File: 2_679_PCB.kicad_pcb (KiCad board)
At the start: 2 copper layers, 101.6 x 76.2 mm, 113 parts, among them J1 POWER_IN, J10 DC Motor Header, J11 DC Motor Header, J12 DC Motor Header, J13 DC Motor Header, J14 Conn_01x06_Female, J15 Conn_01x06_Female, J16 Conn_01x06_Female, J17 Conn_01x06_Female, J18 I2C_3V3, J19 Servo Header, J2 ARDUINO_HEADER_1, J20 Servo Header, J21 Servo Header, J22 Servo Header, J23 Servo Header, J24 Servo Header, J25 Servo Header, J26 Servo Header, J27 RC IN, J28 NEOPIXEL, J29 MPU6050, J3 ARDUINO_HEADER_2, J30 USB_C_Receptacle_USB2.0, J4 I2C_5V, J5 POWER_OUT, J6 DC Motor Header, J7 DC Motor Header, J8 DC Motor Header, J9 DC Motor Header, SW1 SW_SPST, SW2 SW_Push_Open, SW3 SW_P3, SW4 SW_P4, SW5 SW_SPST, U1 SP7652ER-L/TR, U2 AON6558, U3 LMV331, U4 TCA9517DR, U5 AMS1117-5.0, U6 IP2721, U7 BU4SU69G2

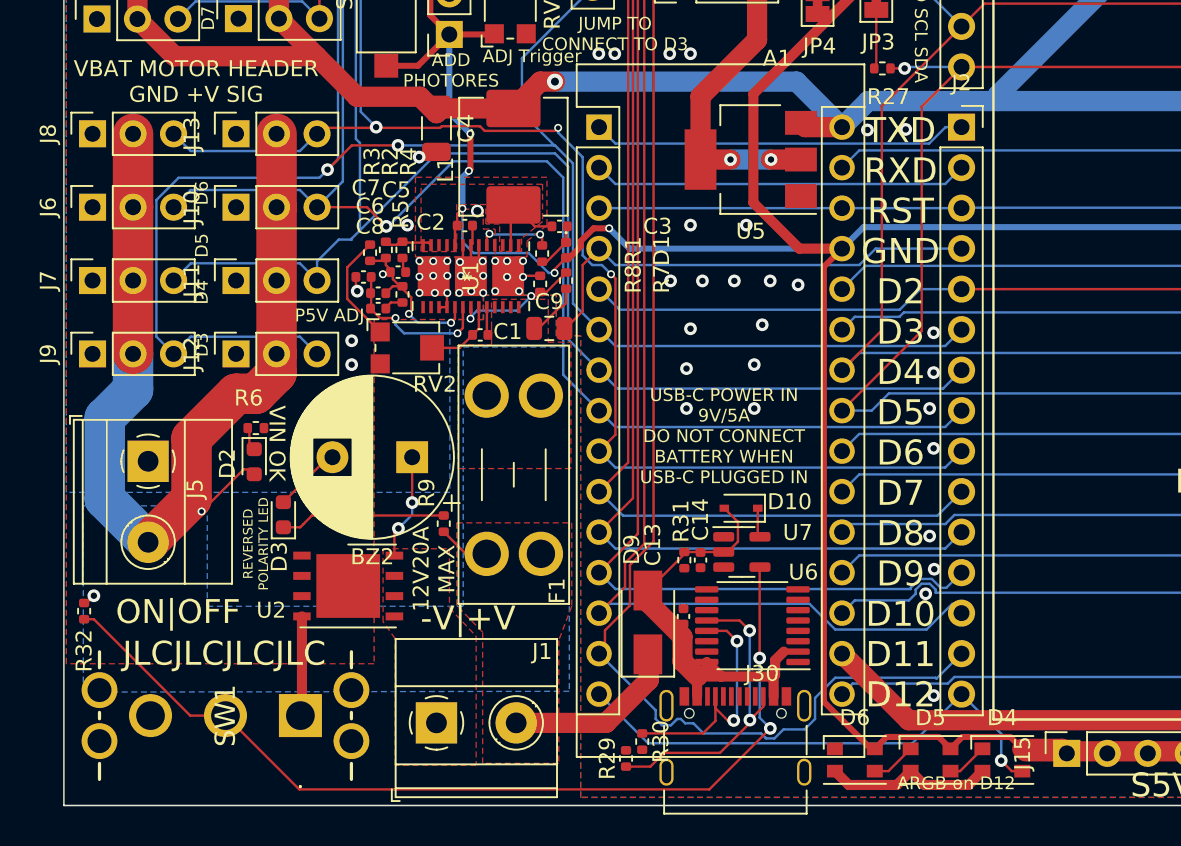
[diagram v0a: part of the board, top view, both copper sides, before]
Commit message: fully defined states for inverter
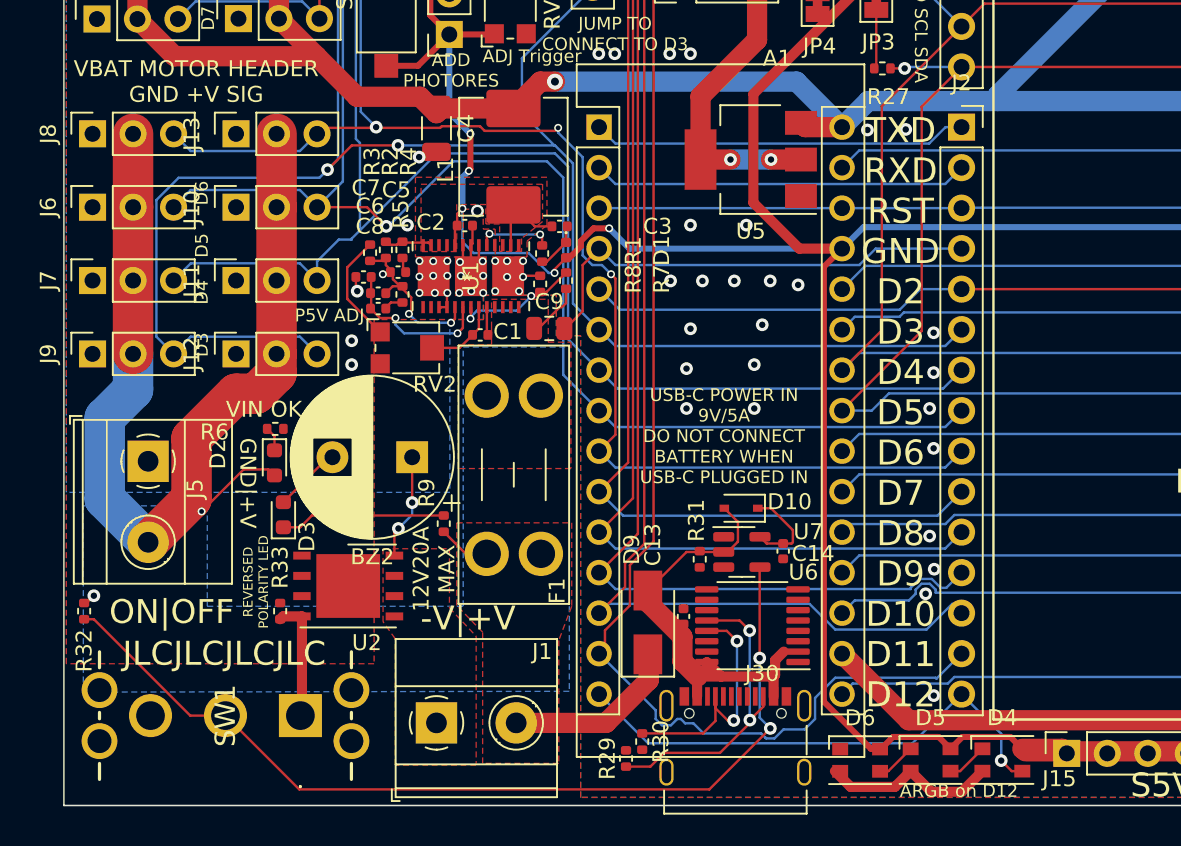
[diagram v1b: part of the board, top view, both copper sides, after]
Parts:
- added G***: LOGO, Logos:pika, B.Cu at (180.5, 117.6)
- added R33: 68K, Resistor_SMD:R_0402_1005Metric, F.Cu at (115.3, 140.2)
- moved C14 5.21 mm to (146.8, 136.4)
- moved D2 1.27 mm to (114.9, 130.9)
- moved R6 1.22 mm to (115.0, 128.8)
- moved R31 0.97 mm to (141.6, 137.0)
- moved D6 0.33 mm to (151.6, 149.6)
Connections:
- C14 pad 2: /VBUS_USBC -> Net-(D10-Pad1)
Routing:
- net Net-(D10-Pad1): track 1.85 -> 6.00 mm
- net VBUS: track 69.8 -> 71.5 mm
- net Net-(SW1-Pad1): track 6.26 -> 7.70 mm
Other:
- board text added: "GND|+V"
- board text added: "MIT / 2.679 / 2.007 Arduino Nano Carrier Board v1.1 2/16/22 WS github.com/wszeto9/2_679_PCB Input Voltage: 7-12V Max Output: 6A @ Vin"
- board text added: "Special note to Danny: This uses a SP7652ER-L/TR Buck IC You can stare at my board all you want but it's a buck IC which is allowed."
- board text added: "Steve: Your only constraint is 3in x 4 in Winnie: So you will print *anything* that fits in that footprint? Steve: Yes...<Looks at this board>"
- board text removed: "I WILL STOP PUTTING PASSIVES TOO CLOSE TO EACH OTHER I WILL STOP PUTTING PASSIVES TOO CLOSE TO EACH OTHER I WILL STOP PUTTING PASSIVES TOO CLOSE TO EACH OTHER I WILL STOP PUTTING PASSIVES TOO CLOSE TO EACH OTHER I WILL STOP PUTTING PASSIVES TOO CLOSE TO EACH OTHER I WILL STOP PUTTING PASSIVES TOO CLOSE TO EACH OTHER I WILL STOP PUTTING PASSIVES TOO CLOSE TO EACH OTHER I WILL STOP PUTTING PASSIVES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"
- board text removed: "MIT / 2.679 / 2.007 Arduino Nano Carrier Board v1.0 2/12/22 WS Input Voltage: 7-12V Max Output: 6A @ Vin"

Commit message: changed e-pads
changed e-pads
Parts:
- R1: value 5.1k -> 5.1R; footprint Resistor_SMD:R_0402_1005Metric -> Resistor_SMD:R_0603_1608Metric
- moved D6 2.24 mm to (153.9, 149.6), turned to -90 degrees
- moved D5 1.37 mm to (157.4, 149.6), turned to -90 degrees
- moved R8 0.82 mm to (131.8, 120.5)
- moved D4 0.43 mm to (161.0, 149.6), turned to -90 degrees
- moved R1 0.25 mm to (131.8, 118.0)
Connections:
- D4 pad 1: Net-(D4-Pad1) -> +5VD
- D4 pad 2: GND -> Net-(D4-Pad2)
- D4 pad 3: /D12 -> GND
- D4 pad 4: +5VD -> /D12
- D5 pad 1: Net-(D5-Pad1) -> +5VD
- D5 pad 2: GND -> Net-(D6-Pad4)
- D5 pad 3: Net-(D4-Pad1) -> GND
- D5 pad 4: +5VD -> Net-(D4-Pad2)
- D6 pad 1: unconnected-(D6-Pad1) -> +5VD
- D6 pad 2: GND -> unconnected-(D6-Pad2)
- D6 pad 3: Net-(D5-Pad1) -> GND
- D6 pad 4: +5VD -> Net-(D6-Pad4)
- U1 pad 28: GND -> /LX
- U1 pad 29: GND -> VBUS
- U2 pad 9: GND -> unconnected-(U2-Pad9)
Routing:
- net Net-(D4-Pad2): track 0.00 -> 3.39 mm
- net Net-(D6-Pad4): track 0.00 -> 3.39 mm
- net GND: track 110.1 -> 107.3 mm, vias 58 -> 45
- net Net-(D5-Pad1): track 2.83 -> 0.00 mm
- net Net-(D4-Pad1): track 2.58 -> 0.00 mm
- net +5VD: track 286.8 -> 289.2 mm
- net /BUCK_ENA: track 7.99 -> 8.75 mm

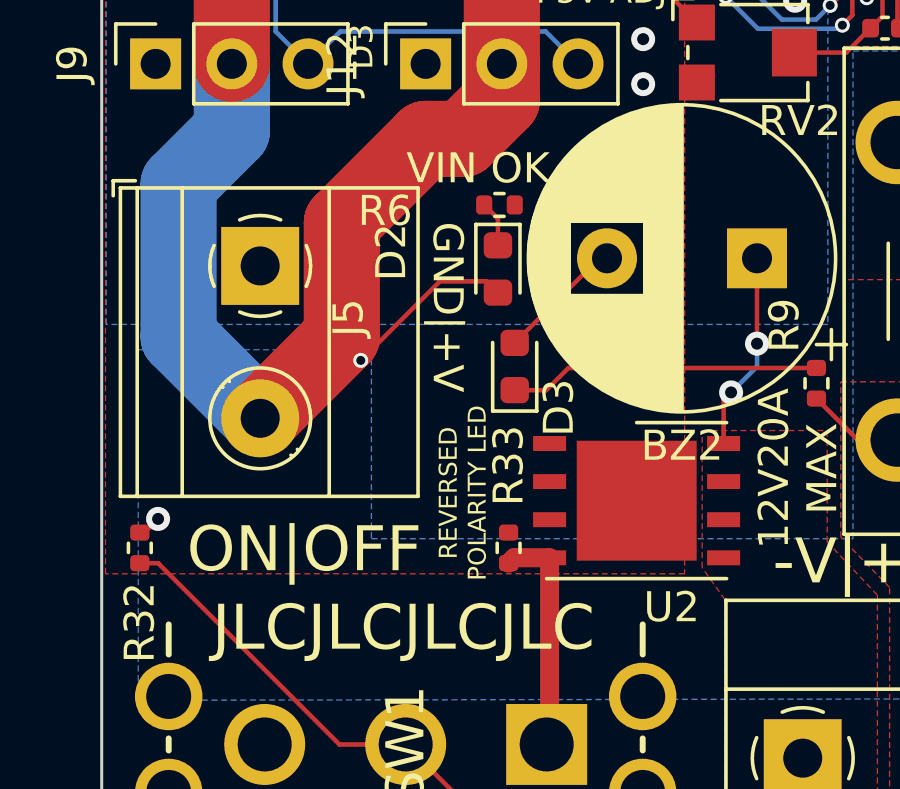
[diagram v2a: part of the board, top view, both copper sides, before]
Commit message: Doubled reverse bias LEDs
Prevents LEDs from blowing up from 5V max reverse bias
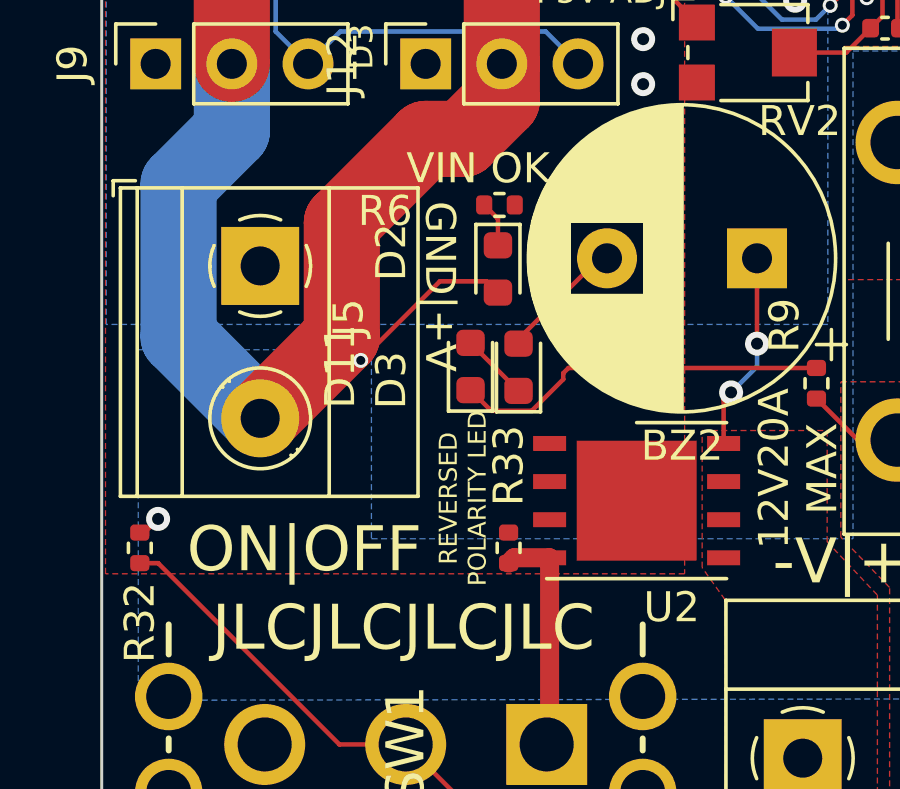
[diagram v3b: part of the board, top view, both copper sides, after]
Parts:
- added D11: LED, LED_SMD:LED_0603_1608Metric, F.Cu at (114.0, 134.2)
- moved D3 0.13 mm to (115.6, 134.2)
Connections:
- R9 pad 1: Net-(D3-Pad1) -> Net-(R9-Pad1)
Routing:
- net Net-(R9-Pad1): track 0.00 -> 12.5 mm
- net Net-(D3-Pad1): track 10.4 -> 2.26 mm
- net Net-(C3-Pad1): track 3.36 -> 0.00 mm
- net +5VD: track 289.2 -> 292.6 mm

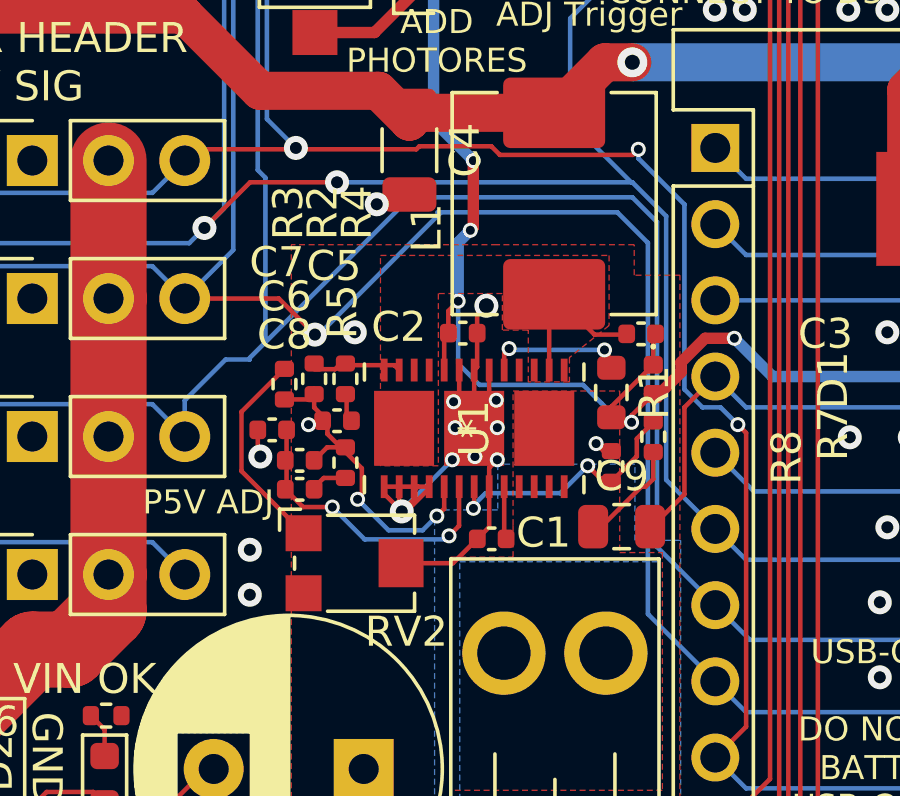
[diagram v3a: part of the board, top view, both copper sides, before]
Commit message: fixed DRC
trace was routed incorrectly
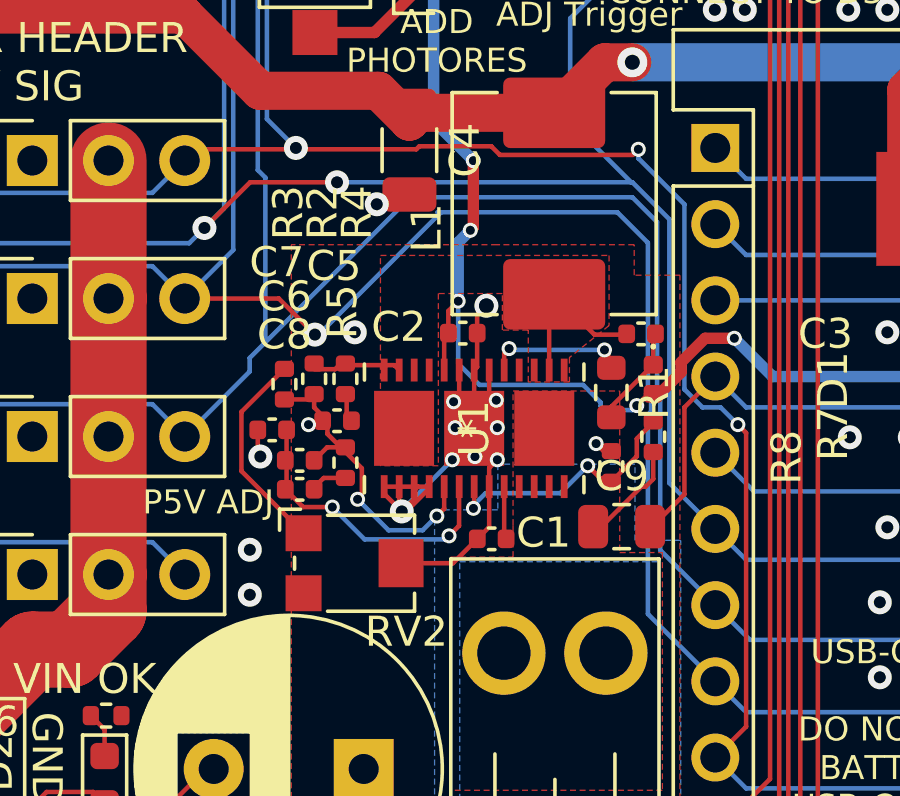
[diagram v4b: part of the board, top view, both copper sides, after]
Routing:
- net +5VD: track 292.6 -> 288.8 mm
- net Net-(C3-Pad1): track 0.00 -> 3.49 mm

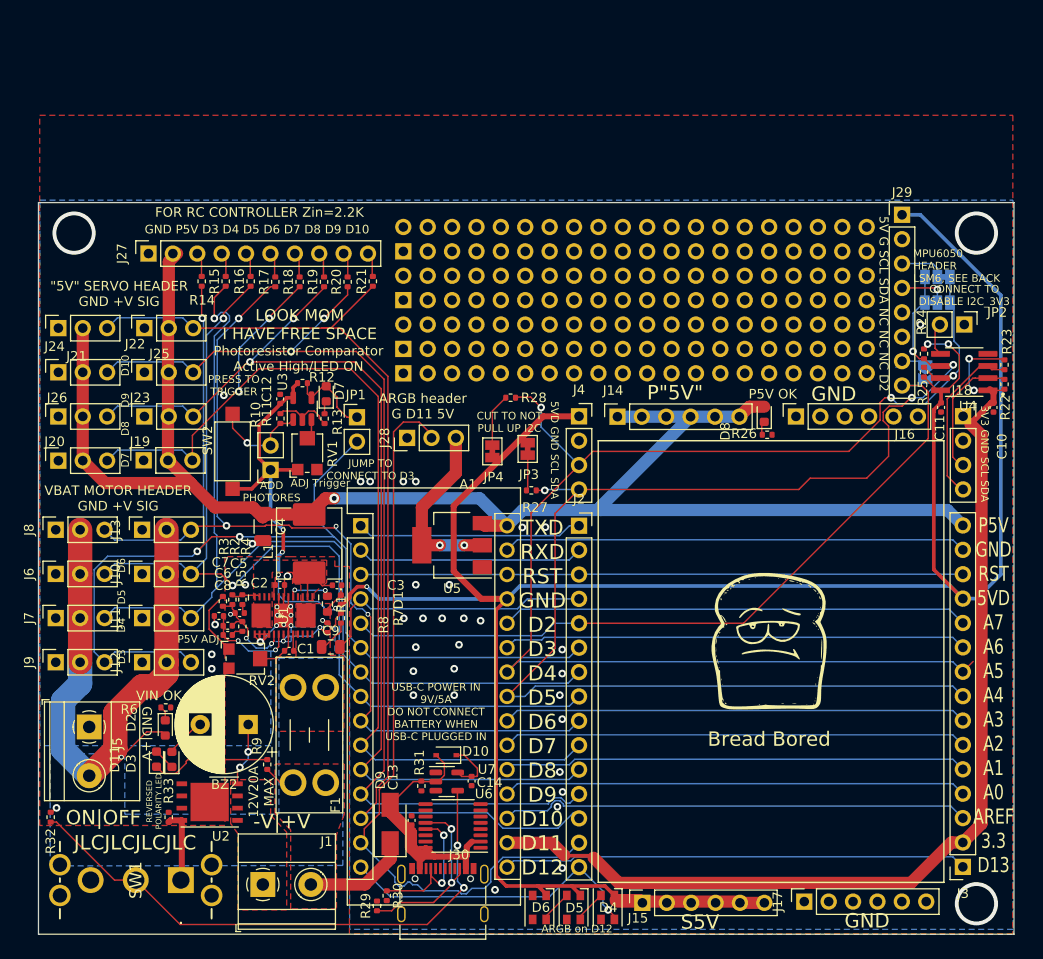
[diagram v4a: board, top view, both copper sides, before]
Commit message: added breakout boards
Added boards to increase space use of the board to 4x4"
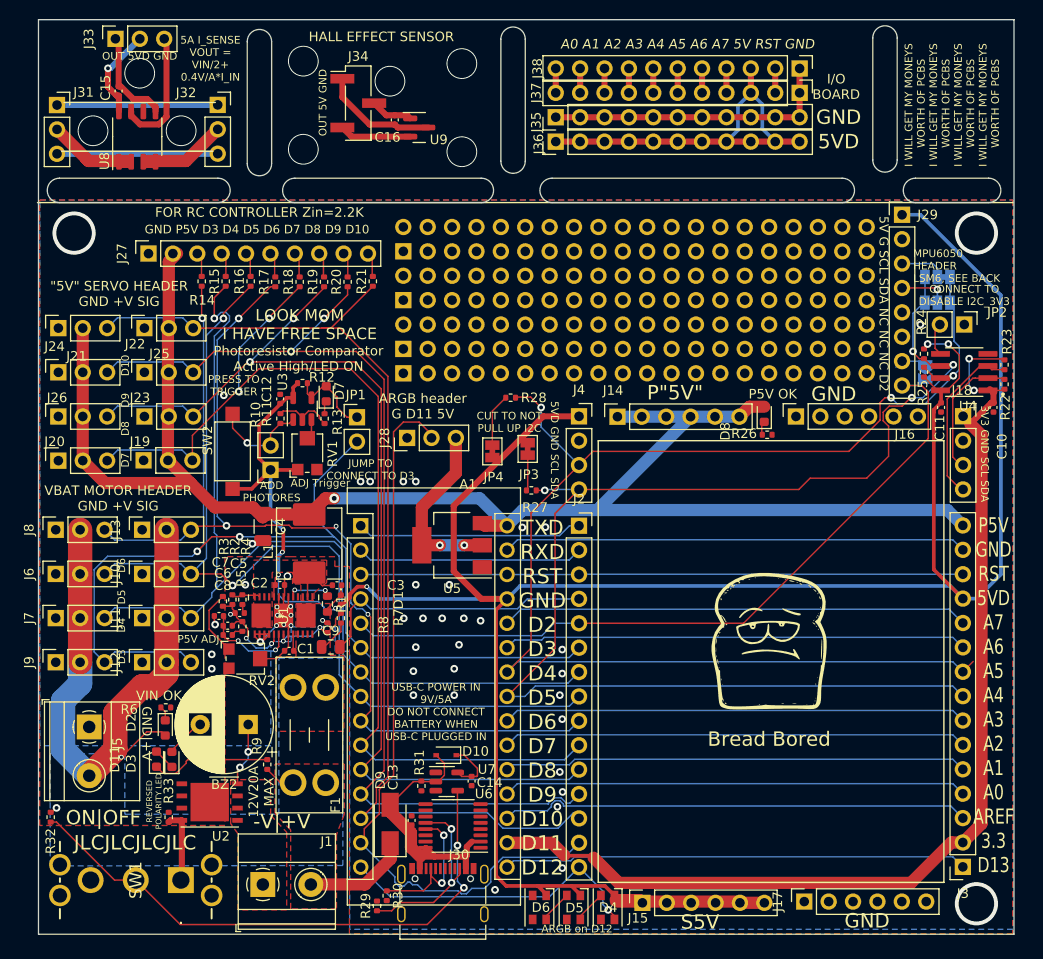
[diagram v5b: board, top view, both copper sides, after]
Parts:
- added C15: 0.1uF, Capacitor_SMD:C_0402_1005Metric, F.Cu at (110.1, 64.6)
- added C16: 0.1uF, Capacitor_SMD:C_0402_1005Metric, F.Cu at (138.8, 67.6)
- added J31: I_IN, Connector_PinSocket_2.54mm:PinSocket_1x03_P2.54mm_Vertical, F.Cu at (103.6, 66.0)
- added J32: I_OUT, Connector_PinSocket_2.54mm:PinSocket_1x03_P2.54mm_Vertical, F.Cu at (120.4, 66.0)
- added J33: D_OUT, Connector_PinSocket_2.54mm:PinSocket_1x03_P2.54mm_Vertical, F.Cu at (109.7, 59.1)
- added J34: HALL_OUT, Connector_PinHeader_2.54mm:PinHeader_1x03_P2.54mm_Vertical_SMD_Pin1Left, F.Cu at (135.0, 65.8)
- added J35: Conn_01x11_Male, Connector_PinHeader_2.54mm:PinHeader_1x11_P2.54mm_Vertical, F.Cu at (155.6, 67.3)
- added J36: Conn_01x11_Male, Connector_PinHeader_2.54mm:PinHeader_1x11_P2.54mm_Vertical, F.Cu at (155.6, 69.8)
- added J37: Conn_01x11_Male, Connector_PinHeader_2.54mm:PinHeader_1x11_P2.54mm_Vertical, F.Cu at (181.0, 64.8)
- added J38: Conn_01x11_Male, Connector_PinHeader_2.54mm:PinHeader_1x11_P2.54mm_Vertical, F.Cu at (181.0, 62.2)
- added U8: CC6920BSO-5A, Package_SO:SOP-8_3.9x4.9mm_P1.27mm, F.Cu at (112.0, 69.3)
- added U9: DRV5033AJxDBZ, Package_TO_SOT_SMD:SOT-23, F.Cu at (141.4, 68.4)
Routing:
- net +5VD: track 288.8 -> 343.1 mm, vias 7 -> 8
- net GND: track 107.3 -> 160.2 mm
- net Net-(J31-Pad3): track 0.00 -> 16.7 mm
- net Net-(J31-Pad1): track 0.00 -> 16.7 mm
- net /OUT: track 0.00 -> 13.0 mm
- net /IP-: track 0.00 -> 9.66 mm
- net /IP+: track 0.00 -> 9.63 mm
- net /HALL_OUT: track 0.00 -> 7.46 mm
- net /A4: track 137.0 -> 139.6 mm
- net /RST: track 62.7 -> 65.3 mm
- net /A7: track 48.7 -> 51.2 mm
- net /A6: track 48.4 -> 50.9 mm
- net /A3: track 48.4 -> 50.9 mm
- net /A2: track 48.4 -> 50.9 mm
- net /A1: track 48.4 -> 50.9 mm
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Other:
- board size 101.6 x 76.2 mm -> 101.6 x 95.2 mm
- board text added: "5A I_SENSE VOUT = VIN/2+ 0.4V/A*I_IN"
- board text added: "5VD"
- board text added: "A0 A1 A2 A3 A4 A5 A6 A7 5V RST GND"
- board text added: "GND 5VD OUT"
- board text added: "HALL EFFECT SENSOR"
- board text added: "I WILL GET MY MONEYS WORTH OF PCBS I WILL GET MY MONEYS WORTH OF PCBS I WILL GET MY MONEYS WORTH OF PCBS I WILL GET MY MONEYS WORTH OF PCBS"
- board text added: "I/O BOARD"
- board text added: "I_IN ON MIDDLE"
- board text added: "MIT / 2.679 / 2.007 Arduino Nano Carrier Board v1.2 2/17/22 WS github.com/wszeto9/2_679_PCB Input Voltage: 7-12V Max Output: 6A @ Vin"
- board text added: "OUT 5V GND"
- board text added: "OUT 5VD GND"
- board text removed: "MIT / 2.679 / 2.007 Arduino Nano Carrier Board v1.1 2/16/22 WS github.com/wszeto9/2_679_PCB Input Voltage: 7-12V Max Output: 6A @ Vin"
